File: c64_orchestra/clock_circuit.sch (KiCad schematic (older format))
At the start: 0 parts

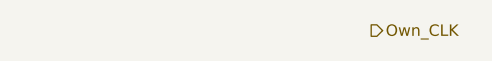
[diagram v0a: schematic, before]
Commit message: Added parts of schematic and worked on pcb layout.
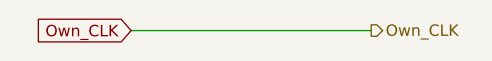
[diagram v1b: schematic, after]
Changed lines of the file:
@@
 Text HLabel 4550 2000 2    50   Output ~ 0
 Own_CLK
+Text GLabel 3500 2000 0    50   Input ~ 0
+Own_CLK
+Wire Wire Line
+	3500 2000 4550 2000
 $EndSCHEMATC
